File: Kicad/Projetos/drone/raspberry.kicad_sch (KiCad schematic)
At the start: 1 part, among them U1 SC0195_9_

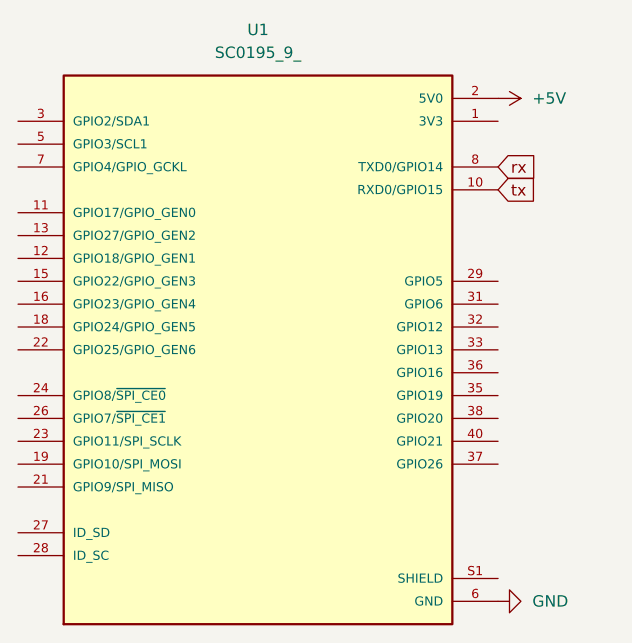
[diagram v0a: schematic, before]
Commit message: capacitores de desacoplamento no kicad
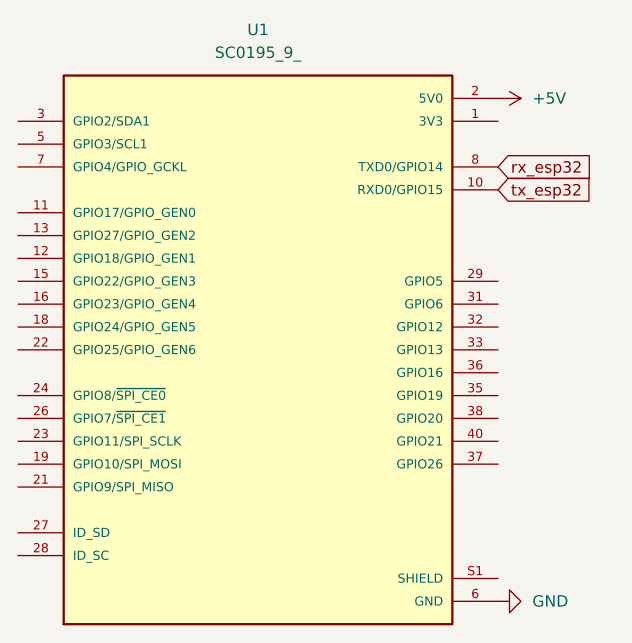
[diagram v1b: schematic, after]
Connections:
- net rx renamed rx_esp32
- net tx renamed tx_esp32
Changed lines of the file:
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@@
 	(generator_version "10.0")
 	(paper "A4")
-	(global_label "tx"
+	(global_label "tx_esp32"
 		(shape input)
 		(at 124.46 66.04 0)
@@
 		)
 		(property "Intersheetrefs" "${INTERSHEET_REFS}"
-			(at 129.199 66.04 0)
+			(at 135.8513 66.04 0)
 			(hide yes)
 			(show_name no)
@@
 		)
 	)
-	(global_label "rx"
+	(global_label "rx_esp32"
 		(shape input)
 		(at 124.46 63.5 0)
@@
 		)
 		(property "Intersheetrefs" "${INTERSHEET_REFS}"
-			(at 129.2595 63.5 0)
+			(at 135.9118 63.5 0)
 			(hide yes)
 			(show_name no)
